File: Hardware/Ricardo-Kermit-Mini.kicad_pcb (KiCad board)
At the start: 4 copper layers, 185 parts, among them IC1 TPS61089RNRR, IC2 AP2205-W5-7, IC3 AP2205-W5-7, IC4 TPS61089RNRR, IC5 ADS131M04IRUKR, J1 RBUS, J2 USB_C_Receptacle_USB2.0, J3 Micro_SD_Card_Det, J4 1053131104, J5 1053131104, J6 1053131104, J7 1053131104, J8 GPIO Breakout, Q1 PMOS, U1 ESP32-S3, U2 SN65HVD230, U3 LM66200DRLR, U4 MAX77827AEFD+T, U5 SC4215, U6 MAX31856, U7 MAX31856, Y1 R940000171

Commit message: wrapping up layout
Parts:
- removed TP10, TP9, TP_CS1, TP_CS2: TestPoint, TestPoint:TestPoint_Pad_D1.0mm
- removed TP4, TP8: TestPoint, TestPoint:TestPoint_Pad_D1.5mm
- added G***: LOGO, iclr:rae_logo_4mm, F.Cu at (67.5, 30.3)
- added G***: LOGO, iclr:iclr_logo_estd2018_6mm, F.Cu at (67.5, 24.7)
- added G***: LOGO, iclr:buffkermit, B.Cu at (46.8, 36.4)
- added G***: LOGO, iclr:TopTrumps, B.Cu at (64.0, 26.4)
- moved J7 241.9 mm to (-2.58, 25.2), turned to 90 degrees
- moved J6 211.7 mm to (26.6, 25.2), turned to 90 degrees
- moved C34 153.5 mm to (4.07, 56.2)
- moved J4 151.5 mm to (12.0, 25.2), turned to 90 degrees
- moved C19 150.0 mm to (11.6, 54.0)
- moved C18 150.0 mm to (11.6, 53.1)
- moved L4 149.9 mm to (2.88, 51.0)
- moved R5 149.8 mm to (10.2, 53.6)
- moved C30 149.7 mm to (13.3, 51.0)
- moved C29 149.7 mm to (11.4, 51.0)
- moved R21 149.6 mm to (9.57, 48.3)
- moved C33 149.5 mm to (8.63, 48.3)
- moved R18 149.5 mm to (9.24, 53.6)
- moved IC1 149.4 mm to (8.87, 51.0)
- moved R19 149.2 mm to (8.29, 54.1)
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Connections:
- C33 pad 1: +3V3 -> RBUS_uC_V
- C34 pad 1: +3V3 -> RBUS_uC_V
- C45 pad 1: +3V3 -> RBUS_uC_V
- C48 pad 1: +3V3 -> RBUS_uC_V
- C56 pad 2: +3.3V -> +3V3
- C57 pad 2: +3.3V -> +3V3
- C61 pad 2: +3.3V -> +3V3
- C62 pad 2: +3.3V -> +3V3
- IC1 pad 9: +3V3 -> RBUS_uC_V
- IC4 pad 9: +3V3 -> RBUS_uC_V
- J1 pad 4: +12V -> DEP
- L4 pad 1: +3V3 -> RBUS_uC_V
- L5 pad 1: +3V3 -> RBUS_uC_V
- R20 pad 2: +3V3 -> RBUS_uC_V
- R29 pad 2: +3V3 -> RBUS_uC_V
- R7 pad 1: +12V -> DEP
- U1 pad 16: /CS0 -> /CS1
- U1 pad 17: /CS1 -> /CS0
- U1 pad 41: unconnected-(U1-GPIO36-Pad41) -> /ADS_CS0
- U1 pad 42: /ADS_CS0 -> unconnected-(U1-GPIO37-Pad42)
- U1 pad 47: unconnected-(U1-MTDI/JTAG/GPIO41-Pad47) -> /CAN_RX
- U1 pad 48: unconnected-(U1-MTMS/JTAG/GPIO42-Pad48) -> /CAN_TX
- U6 pad 5: +3.3V -> +3V3
- U6 pad 8: +3.3V -> +3V3
- U7 pad 5: +3.3V -> +3V3
- U7 pad 8: +3.3V -> +3V3
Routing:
- net +5V: track 3.91 -> 88.4 mm, vias 0 -> 2
- net +12V: track 0.00 -> 80.4 mm, vias 0 -> 5
- net RBUS_uC_V: track 0.00 -> 78.8 mm, vias 0 -> 2
- net /HSPI_SCLK: track 0.00 -> 51.4 mm, vias 0 -> 3
- net /HSPI_MISO: track 0.00 -> 50.3 mm, vias 0 -> 3
- net /HSPI_MOSI: track 0.00 -> 48.8 mm, vias 0 -> 3
- net /SD1_DET: track 0.00 -> 38.6 mm
- net /CS1: track 0.00 -> 35.5 mm, vias 0 -> 2
- net +3V3: track 3.89 -> 39.1 mm, vias 1 -> 17
- net /pressure_sensor1/AIN0N: track 0.00 -> 30.8 mm, vias 0 -> 2
- net /VSPI_MISO: track 0.00 -> 30.6 mm
- net /VSPI_SCLK: track 0.00 -> 30.0 mm
- net /SD_EN: track 0.00 -> 29.1 mm, vias 0 -> 2
- net /Data-: track 0.00 -> 28.8 mm
- net /VSPI_MOSI: track 0.00 -> 28.5 mm
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- added copper zone on In2.Cu, net +3V3
- added copper zone on F.Cu, net /Boosts1/LDO12V_IN
- added copper zone on F.Cu, net /Boosts1/LDO5.5V_IN
- added copper zone on B.Cu, net GND
- added copper zone on In1.Cu, net GND
- added copper zone on F.Cu, net Net-(IC1-SW)
- added copper zone on F.Cu, net Net-(IC4-SW)
- added copper zone on F.Cu, net RBUS_uC_V
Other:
- board outline added: 84 x 43 mm
- board text added: "12V"
- board text added: "3V3"
- board text added: "5V"
- board text added: "ADC0"
- board text added: "ADC1"
- board text added: "ADC2"
- board text added: "ADC3"
- board text added: "BOOT"
- board text added: "Current"
- board text added: "D+"
- board text added: "D-"
- board text added: "DEP"
- board text added: "EN"
- board text added: "GPIO"
- board text added: "RBUS"
- board text added: "TC1"
- board text added: "TC2"
- board text added: "TX"
- board text added: "USB"
- board text added: "Voltage"

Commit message: layout
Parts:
- added CANRXLED1: CANRXLED, LED_SMD:LED_0402_1005Metric, F.Cu at (20.5, 42.6)
- added CANTXLED1: CANTXLED, LED_SMD:LED_0402_1005Metric, F.Cu at (20.5, 46.5)
- added G***: LOGO, iclr:rae_logo_8mm, B.Cu at (59.1, 47.4)
- added G***: LOGO, iclr:iclr_logo_estd2018_10mm, B.Cu at (59.5, 35.6)
- added R55: 1k, Resistor_SMD:R_0402_1005Metric, F.Cu at (21.4, 46.5)
- added R56: 1k, Resistor_SMD:R_0402_1005Metric, F.Cu at (21.4, 41.6)
- moved G*** 69.3 mm to (-5.17, 29.8), turned to -90 degrees
- moved G*** 34.8 mm to (12.2, 40.4), turned to -90 degrees
- moved R2 1.11 mm to (21.3, 48.9)
- moved TXLED1 1.11 mm to (21.3, 47.9)
- moved R47 0.62 mm to (-1.82, 28.8)
- moved R38 0.55 mm to (11.7, 28.8)
- moved R39 0.35 mm to (41.0, 28.8)
- moved R46 0.29 mm to (27.3, 28.8)
- moved C50 0.27 mm to (26.6, 35.4)
- moved C51 0.25 mm to (26.6, 36.3)
- moved C52 0.10 mm to (26.5, 37.7)
- moved R18 0.05 mm to (9.29, 53.6)
- moved R19 0.05 mm to (8.35, 54.1)
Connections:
- J8 pad 9: /5V -> +5V
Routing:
- net +5V: track 88.4 -> 111.2 mm, vias 2 -> 3
- net GND: track 10.1 -> 11.9 mm, vias 91 -> 133
- net +3V3: track 39.1 -> 40.6 mm, vias 17 -> 19
- net /TXD: track 6.95 -> 8.10 mm
- net Net-(CANTXLED1-A): track 0.00 -> 0.96 mm
- net Net-(CANRXLED1-A): track 0.00 -> 0.94 mm
- net /CAN_TX: track 11.2 -> 11.9 mm
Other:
- board text added: "+"
- board text added: "-"
- board text added: "CAN"
- board text added: "Designed by Electronics 2024"
- board text added: "IV I am 69 1.989e+30 84 x 43 Mini Yes 420"
- board text added: "K - Kerbal E - ESP32 R - Regressed M - Mission I - with Integrated T - Thermocouples"
- board text added: "Power Speed Skills Bench (kg) Dimensions (mm) Version Mrs Piggy Top Trumps Rating"
- board text added: "RX"
- board text added: "◂GND"

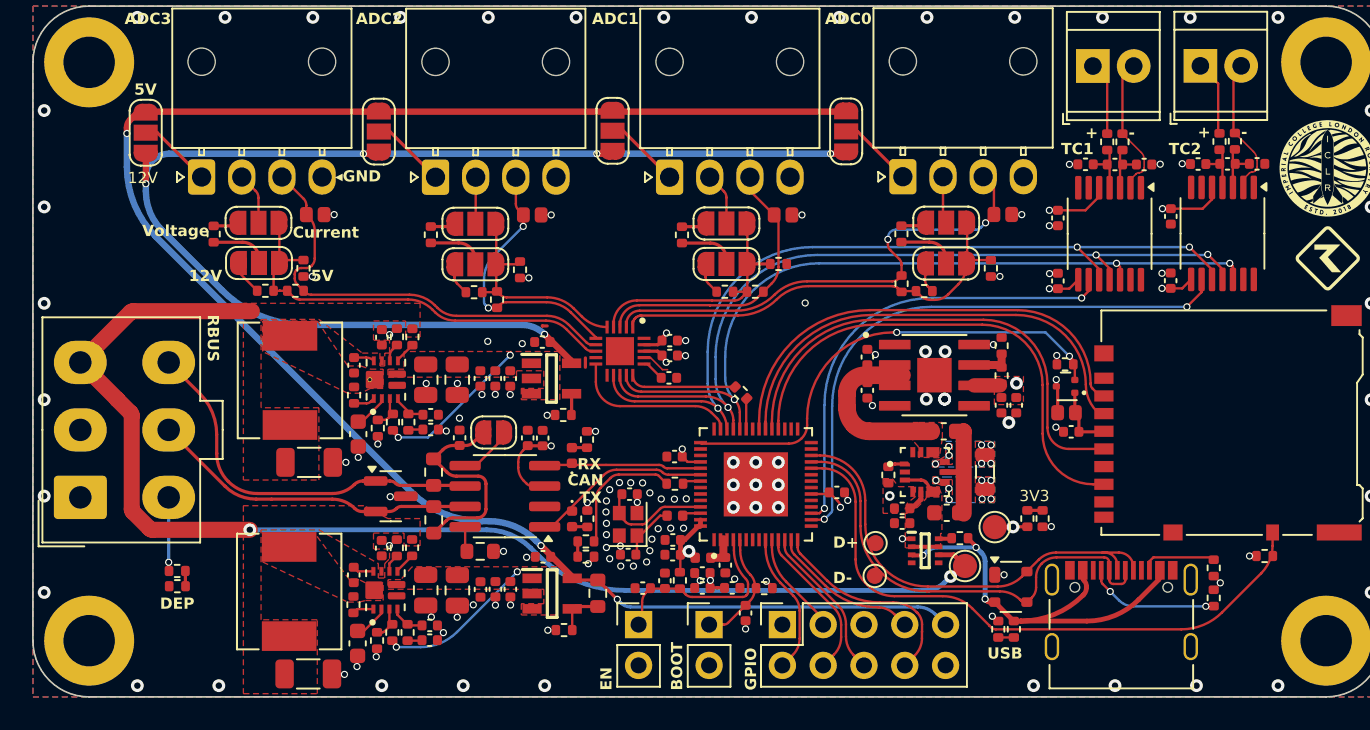
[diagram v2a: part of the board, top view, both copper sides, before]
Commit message: added diodes on gpio breakout and sensor supply
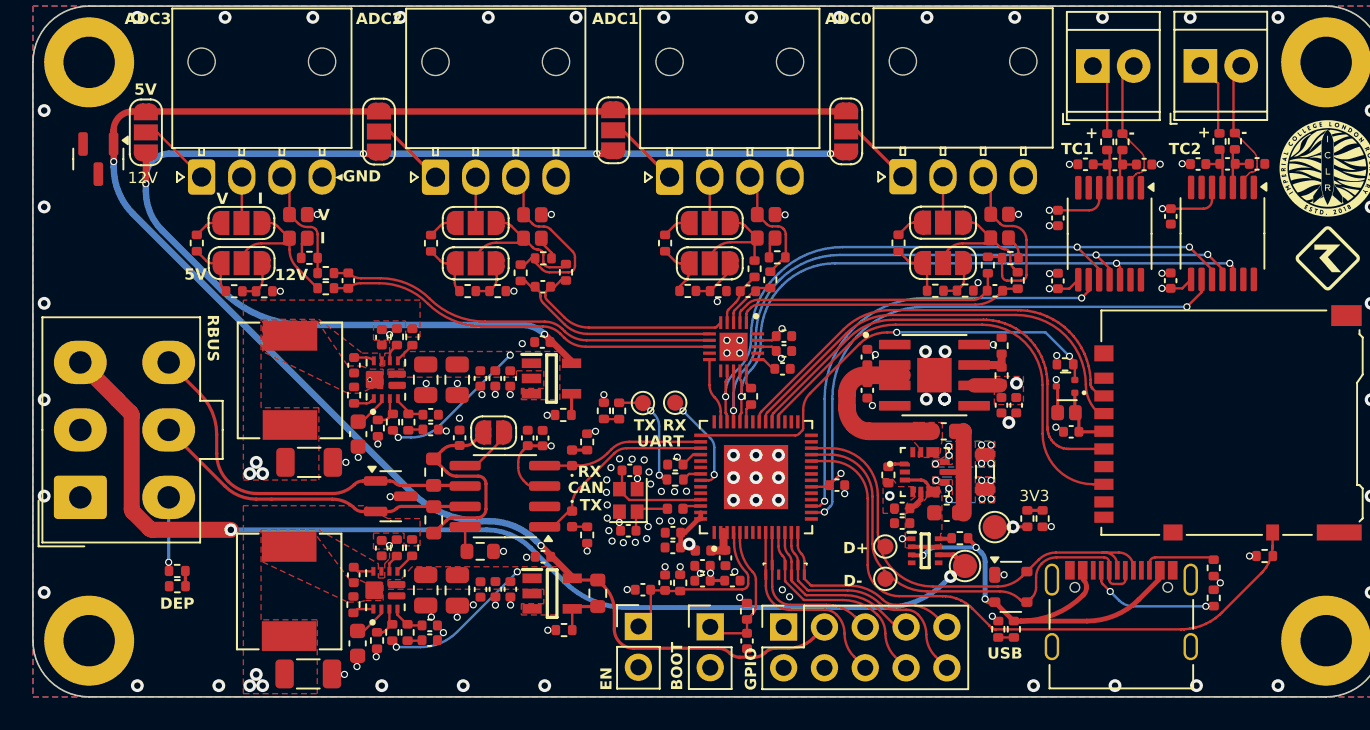
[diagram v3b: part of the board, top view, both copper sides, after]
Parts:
- added C63: 10nF, Capacitor_SMD:C_0402_1005Metric, F.Cu at (46.8, 32.3)
- added C64: 10nF, Capacitor_SMD:C_0402_1005Metric, F.Cu at (31.4, 32.3)
- added C65: 10nF, Capacitor_SMD:C_0402_1005Metric, F.Cu at (18.7, 32.1)
- added C66: 10nF, Capacitor_SMD:C_0402_1005Metric, F.Cu at (6.55, 31.7)
- added D3: MMBZ6V2ALT1G, Package_TO_SOT_SMD:SOT-23, F.Cu at (-9.01, 24.1)
- added D6: RCLAMP3346PQTNT, iclr:RCLAMP3346PQTNT, F.Cu at (33.7, 49.7)
- added JP19: SolderJumper_2_Open, iclr:SmallerSolderJP, F.Cu at (46.8, 29.0)
- added JP20: SolderJumper_3_Open, Jumper:SolderJumper-3_P1.3mm_Open_RoundedPad1.0x1.5mm_NumberLabels, F.Cu at (23.0, 22.3)
- added JP21: SolderJumper_2_Open, iclr:SmallerSolderJP, F.Cu at (3.17, 27.6)
- added JP22: SolderJumper_3_Open, Jumper:SolderJumper-3_P1.3mm_Open_RoundedPad1.0x1.5mm_NumberLabels, F.Cu at (-6.04, 22.4)
- added R57: 1k, Resistor_SMD:R_0402_1005Metric, F.Cu at (48.2, 31.7)
- added R58: 1k, Resistor_SMD:R_0402_1005Metric, F.Cu at (46.4, 30.7)
- added R59: 49, Resistor_SMD:R_0402_1005Metric, F.Cu at (33.3, 30.2)
- added R60: 1k, Resistor_SMD:R_0402_1005Metric, F.Cu at (32.8, 31.6)
- added R61: 10k, Resistor_SMD:R_0402_1005Metric, F.Cu at (1.32, 32.3)
- added R62: 1k, Resistor_SMD:R_0402_1005Metric, F.Cu at (5.16, 32.1)
- added R63: 49, Resistor_SMD:R_0402_1005Metric, F.Cu at (4.13, 30.3)
- added R64: 1k, Resistor_SMD:R_0402_1005Metric, F.Cu at (5.16, 31.2)
- added TP3: TestPoint, TestPoint:TestPoint_Pad_D1.0mm, F.Cu at (24.9, 39.3)
- added TP4: TestPoint, TestPoint:TestPoint_Pad_D1.0mm, F.Cu at (26.9, 39.3)
- JP16, JP18, JP9: value SolderJumper_3_Open -> SolderJumper_2_Open; footprint Jumper:SolderJumper-3_P1.3mm_Open_RoundedPad1.0x1.5mm_NumberLabels -> iclr:SmallerSolderJP
- JP17: value SolderJumper_2_Open -> SolderJumper_3_Open; footprint iclr:SmallerSolderJP -> Jumper:SolderJumper-3_P1.3mm_Open_RoundedPad1.0x1.5mm_NumberLabels
- R34, R35, R42: value 58.4k -> 75k
- R36, R43: value 10k -> 14k
- R38, R46: value 31.6k -> 10k
- R39: value 31.6k -> 14k
- R40, R48: value 49 -> 1k
- R44: value 58.4k -> 49
- R45: value 10k -> 1k
- R47: value 31.6k -> 75k
- R49: value 49 -> 14k
- moved R44 17.4 mm to (18.7, 30.3), turned to 180 degrees
- moved R45 13.5 mm to (17.3, 31.2), turned to -90 degrees
- moved JP18 11.3 mm to (3.17, 29.0), turned to 180 degrees
- moved JP16 10.7 mm to (32.3, 27.6), turned to 180 degrees
- moved JP9 10.6 mm to (17.7, 27.6), turned to 180 degrees
- moved JP13 9.41 mm to (8.46, 22.4), turned to -90 degrees
- moved R2 9.15 mm to (22.5, 39.8), turned to -90 degrees
- moved TXLED1 8.38 mm to (23.4, 39.8), turned to -90 degrees
- moved C50 7.12 mm to (33.7, 35.1)
- moved C51 7.12 mm to (33.7, 36.1)
- moved C52 7.09 mm to (33.6, 37.2)
- moved IC5 7.08 mm to (30.5, 35.8)
- moved R41 6.96 mm to (47.8, 30.3), turned to 180 degrees
- moved R43 5.89 mm to (27.7, 32.3), turned to 0 degrees
- moved R38 5.44 mm to (15.9, 32.3), turned to 180 degrees
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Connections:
- net /Boosts1/FB_12V renamed /Boosts/FB_12V
- net /Boosts1/FB_5V renamed /Boosts/FB_5V
- net /Boosts1/LDO12V_IN renamed /Boosts/LDO12V_IN
- net /Boosts1/LDO5.5V_IN renamed /Boosts/LDO5.5V_IN
- net /Boosts1/SW_12V renamed /Boosts/SW_12V
- net /Boosts1/SW_5V renamed /Boosts/SW_5V
- C33 pad 1: RBUS_uC_V -> +3V3
- C34 pad 1: RBUS_uC_V -> +3V3
- C45 pad 1: RBUS_uC_V -> +3V3
- C48 pad 1: RBUS_uC_V -> +3V3
- IC1 pad 9: RBUS_uC_V -> +3V3
- IC4 pad 9: RBUS_uC_V -> +3V3
- IC5 pad 21: unconnected-(IC5-EP-Pad21) -> GND
- J4 pad 1: Net-(JP9-C) -> Net-(JP13-C)
- J4 pad 2: Net-(JP3-C) -> Net-(JP4-C)
- J4 pad 3: /pressure_sensor1/AIN2N -> Net-(JP9-B)
- J5 pad 3: /pressure_sensor1/AIN0N -> Net-(JP8-B)
- J6 pad 1: Net-(JP16-C) -> Net-(JP20-C)
- J6 pad 2: Net-(JP11-C) -> Net-(JP12-C)
- J6 pad 3: /pressure_sensor1/AIN1N -> Net-(JP16-B)
- J7 pad 1: Net-(JP18-C) -> Net-(JP22-C)
- J7 pad 2: Net-(JP13-C) -> Net-(JP17-C)
- J7 pad 3: /pressure_sensor1/AIN3N -> Net-(JP21-B)
- J8 pad 10: GND -> /GPIO8
- J8 pad 2: /GPIO4 -> GND
- J8 pad 3: /GPIO5 -> +5V
- J8 pad 4: /GPIO6 -> +3V3
- J8 pad 5: +3V3 -> /GPIO5
- J8 pad 6: /GPIO7 -> /GPIO4
- J8 pad 7: /GPIO8 -> /GPIO7
- J8 pad 8: /GPIO9 -> /GPIO6
- J8 pad 9: +5V -> /GPIO9
- JP11 pad 3: /pressure_sensor1/AIN1P -> Net-(JP11-B)
- JP12 pad 1: /pressure_sensor1/AIN1P -> Net-(JP11-C)
- JP13 pad 1: Net-(JP13-A) -> +5V
- JP13 pad 3: /pressure_sensor1/AIN3P -> +12V
- JP14 pad 1: /pressure_sensor1/AIN3P -> Net-(JP14-A)
- JP15 pad 1: GND -> Net-(JP15-A)
- JP15 pad 2: /pressure_sensor1/AIN1N -> Net-(JP11-C)
- JP16 pad 1: +5V -> GND
- JP16 pad 2: Net-(JP16-C) -> Net-(JP16-B)
- JP17 pad 1: GND -> Net-(JP14-C)
- JP17 pad 2: /pressure_sensor1/AIN3N -> Net-(JP17-C)
- JP18 pad 1: +5V -> Net-(JP18-A)
- JP18 pad 2: Net-(JP18-C) -> Net-(JP14-C)
- JP3 pad 3: /pressure_sensor1/AIN2P -> Net-(JP3-B)
- JP4 pad 1: /pressure_sensor1/AIN2P -> Net-(JP3-C)
- JP5 pad 1: Net-(JP5-A) -> Net-(JP19-B)
- JP5 pad 3: /pressure_sensor1/AIN0P -> Net-(JP5-B)
- JP6 pad 1: /pressure_sensor1/AIN0P -> Net-(JP6-A)
- JP6 pad 2: Net-(JP6-C) -> Net-(JP19-B)
- JP7 pad 1: GND -> Net-(JP7-A)
- JP7 pad 2: /pressure_sensor1/AIN2N -> Net-(JP3-C)
- JP8 pad 2: /pressure_sensor1/AIN0N -> Net-(JP8-B)
- JP9 pad 1: +5V -> GND
- JP9 pad 2: Net-(JP9-C) -> Net-(JP9-B)
- L4 pad 1: RBUS_uC_V -> +3V3
- L5 pad 1: RBUS_uC_V -> +3V3
- R20 pad 2: RBUS_uC_V -> +3V3
- R29 pad 2: RBUS_uC_V -> +3V3
- R34 pad 2: /pressure_sensor1/AIN2P -> Net-(JP3-B)
- R35 pad 1: Net-(JP6-B) -> Net-(JP5-B)
- R35 pad 2: /pressure_sensor1/AIN0P -> Net-(JP6-B)
- R36 pad 1: GND -> Net-(JP3-B)
- R36 pad 2: /pressure_sensor1/AIN2P -> Net-(JP3-A)
- R37 pad 2: /pressure_sensor1/AIN0P -> Net-(JP6-A)
- R38 pad 1: Net-(JP3-A) -> GND
- R38 pad 2: Net-(JP4-C) -> Net-(JP3-A)
- R39 pad 1: Net-(JP5-A) -> Net-(JP6-B)
- R39 pad 2: Net-(JP6-C) -> Net-(JP6-A)
- R40 pad 1: /pressure_sensor1/AIN2P -> Net-(JP3-C)
- R40 pad 2: /pressure_sensor1/AIN2N -> /pressure_sensor1/AIN2P
- R41 pad 1: /pressure_sensor1/AIN0P -> Net-(JP19-A)
- R41 pad 2: /pressure_sensor1/AIN0N -> Net-(JP8-B)
- R42 pad 2: /pressure_sensor1/AIN1P -> Net-(JP11-B)
- R43 pad 1: GND -> Net-(JP11-B)
- R43 pad 2: /pressure_sensor1/AIN1P -> Net-(JP11-A)
- R44 pad 1: Net-(JP14-B) -> Net-(JP7-A)
- R44 pad 2: /pressure_sensor1/AIN3P -> Net-(JP9-B)
- R45 pad 1: GND -> Net-(JP9-B)
- R45 pad 2: /pressure_sensor1/AIN3P -> /pressure_sensor1/AIN2N
- R46 pad 1: Net-(JP11-A) -> GND
- R46 pad 2: Net-(JP12-C) -> Net-(JP11-A)
- R47 pad 1: Net-(JP13-A) -> Net-(JP17-B)
- R47 pad 2: Net-(JP14-C) -> Net-(JP14-B)
- R48 pad 1: /pressure_sensor1/AIN1P -> Net-(JP11-C)
- R48 pad 2: /pressure_sensor1/AIN1N -> /pressure_sensor1/AIN1P
- R49 pad 1: /pressure_sensor1/AIN3P -> Net-(JP14-B)
- R49 pad 2: /pressure_sensor1/AIN3N -> Net-(JP14-A)
- U1 pad 44: unconnected-(U1-MTCK/JTAG/GPIO39-Pad44) -> /CAN_RX
- U1 pad 45: unconnected-(U1-MTDO/JTAG/GPIO40-Pad45) -> /CAN_TX
- U1 pad 47: /CAN_RX -> unconnected-(U1-MTDI/JTAG/GPIO41-Pad47)
- U1 pad 48: /CAN_TX -> unconnected-(U1-MTMS/JTAG/GPIO42-Pad48)
- U6 pad 13: /thermocouple2/FAULT -> /thermocouple1/FAULT
- U6 pad 7: /thermocouple2/DRDY -> /thermocouple1/DRDY
- U7 pad 13: /thermocouple3/FAULT -> /thermocouple2/FAULT
- U7 pad 7: /thermocouple3/DRDY -> /thermocouple2/DRDY
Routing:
- net /pressure_sensor1/AIN1N: track 18.2 -> 3.57 mm
- net /pressure_sensor1/AIN0N: track 30.9 -> 17.6 mm, vias 2 -> 0
- net /pressure_sensor1/AIN1P: track 16.1 -> 3.49 mm
- net Net-(JP9-B): track 0.00 -> 11.6 mm
- net Net-(JP8-B): track 0.00 -> 11.6 mm
- net RBUS_uC_V: track 78.3 -> 67.2 mm
- net /pressure_sensor1/AIN0P: track 27.4 -> 18.0 mm
- net Net-(JP19-B): track 0.00 -> 8.71 mm
- net /HSPI_SCLK: track 51.4 -> 43.0 mm
- net /HSPI_MOSI: track 48.8 -> 41.2 mm
- net Net-(JP16-B): track 0.00 -> 7.60 mm
- net /HSPI_MISO: track 50.4 -> 42.9 mm
- net Net-(JP21-B): track 0.00 -> 7.24 mm
- net Net-(JP3-C): track 2.91 -> 9.59 mm
- net /RXD: track 0.00 -> 6.48 mm, vias 0 -> 2
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- removed copper zone on F.Cu, net RBUS_uC_V
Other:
- board text added: "I"
- board text added: "UART"
- board text added: "V"
- board text removed: "Current"
- board text removed: "Voltage"

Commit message: silkscreen changes
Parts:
- moved G*** 3.71 mm to (59.2, 31.9)
- moved G*** 1.90 mm to (59.1, 49.3)
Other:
- board text added: "Designed by Shiven Chandarana Artem Sheykin"
- board text added: "RAE 2024"
- board text removed: "Designed by Electronics 2024"
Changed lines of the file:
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@@
 	(footprint "iclr:rae_logo_8mm"
 		(layer "B.Cu")
-		(at 59.125 47.39 -90)
+		(at 59.125 49.29 -90)
 		(property "Reference" "G***"
 			(at 0 0 90)
@@
 	(footprint "iclr:iclr_logo_estd2018_10mm"
 		(layer "B.Cu")
-		(at 59.525 35.59 -90)
+		(at 59.225 31.89 -90)
 		(property "Reference" "G***"
 			(at 0 0 90)
@@
 		)
 	)
-	(gr_text "Designed by \nElectronics 2024"
-		(at 67.825 42.19 90)
+	(gr_text "Designed by \nShiven Chandarana\nArtem Sheykin"
+		(at 68.725 41.29 90)
 		(layer "B.SilkS")
 		(effects
@@
 		)
 	)
+	(gr_text "RAE 2024"
+		(at 59.725 41.19 90)
+		(layer "B.SilkS")
+		(effects
+			(font
+				(size 1 1)
+				(thickness 0.15)
+			)
+			(justify bottom mirror)
+		)
+	)
